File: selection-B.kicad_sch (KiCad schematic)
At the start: 11 parts, among them Q2 Q_NMOS_DGS, Q3 Q_NMOS_DGS, Q4 Q_NMOS_DGS, Q5 Q_NMOS_DGS, U11 SN74LS08N, U12 SN74LS08N, U13 CD74HCT32E, U9 SN74LS08N

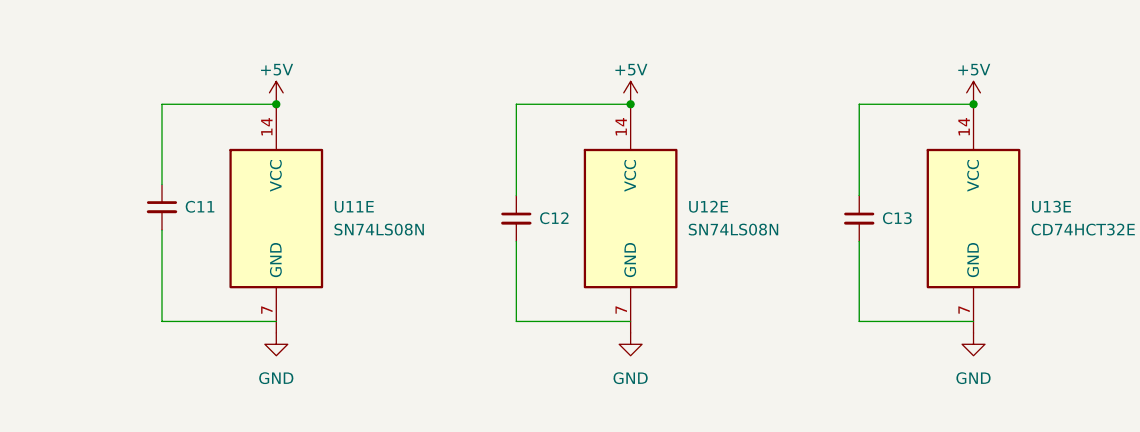
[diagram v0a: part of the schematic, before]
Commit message: fix: fixed link of capas
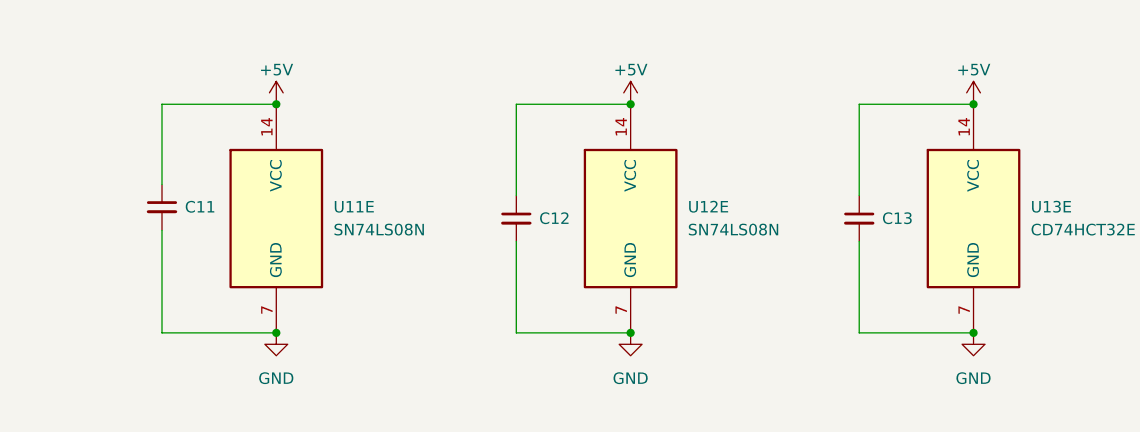
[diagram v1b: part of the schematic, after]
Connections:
- net GND: now also C11.2, C12.2, C13.2
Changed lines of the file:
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@@
+	)
+	(junction
+		(at 265.43 156.21)
+		(diameter 0)
+		(color 0 0 0 0)
+	)
+	(junction
+		(at 187.96 156.21)
+		(diameter 0)
+		(color 0 0 0 0)
 	)
 	(junction
@@
 		(color 0 0 0 0)
 	)
+	(junction
+		(at 227.33 156.21)
+		(diameter 0)
+		(color 0 0 0 0)
+	)
 	(wire
 		(pts
@@
 	(wire
 		(pts
-			(xy 187.96 154.94) (xy 175.26 154.94)
-		)
-		(stroke
-			(width 0)
-			(type default)
-		)
-	)
-	(wire
-		(pts
 			(xy 62.23 48.26) (xy 80.01 48.26)
 		)
@@
 	(wire
 		(pts
+			(xy 252.73 146.05) (xy 252.73 156.21)
+		)
+		(stroke
+			(width 0)
+			(type default)
+		)
+	)
+	(wire
+		(pts
 			(xy 101.6 93.98) (xy 105.41 93.98)
 		)
@@
 	(wire
 		(pts
-			(xy 175.26 154.94) (xy 175.26 144.78)
-		)
-		(stroke
-			(width 0)
-			(type default)
-		)
-	)
-	(wire
-		(pts
 			(xy 99.06 80.01) (xy 99.06 107.95)
 		)
@@
 	(wire
 		(pts
+			(xy 175.26 144.78) (xy 175.26 156.21)
+		)
+		(stroke
+			(width 0)
+			(type default)
+		)
+	)
+	(wire
+		(pts
 			(xy 101.6 38.1) (xy 105.41 38.1)
 		)
@@
 	(wire
 		(pts
-			(xy 252.73 154.94) (xy 252.73 146.05)
-		)
-		(stroke
-			(width 0)
-			(type default)
-		)
-	)
-	(wire
-		(pts
 			(xy 87.63 71.12) (xy 91.44 71.12)
 		)
@@
 	(wire
 		(pts
-			(xy 214.63 154.94) (xy 214.63 146.05)
-		)
-		(stroke
-			(width 0)
-			(type default)
-		)
-	)
-	(wire
-		(pts
 			(xy 124.46 49.53) (xy 120.65 49.53)
 		)
@@
 	(wire
 		(pts
+			(xy 214.63 146.05) (xy 214.63 156.21)
+		)
+		(stroke
+			(width 0)
+			(type default)
+		)
+	)
+	(wire
+		(pts
 			(xy 59.69 17.78) (xy 73.66 17.78)
 		)
@@
 	(wire
 		(pts
-			(xy 227.33 154.94) (xy 214.63 154.94)
-		)
-		(stroke
-			(width 0)
-			(type default)
-		)
-	)
-	(wire
-		(pts
 			(xy 99.06 52.07) (xy 105.41 52.07)
 		)
@@
 	(wire
 		(pts
-			(xy 265.43 154.94) (xy 252.73 154.94)
-		)
-		(stroke
-			(width 0)
-			(type default)
-		)
-	)
-	(wire
-		(pts
 			(xy 69.85 88.9) (xy 69.85 104.14)
 		)
@@
 	(wire
 		(pts
+			(xy 252.73 156.21) (xy 265.43 156.21)
+		)
+		(stroke
+			(width 0)
+			(type default)
+		)
+	)
+	(wire
+		(pts
 			(xy 139.7 69.85) (xy 143.51 69.85)
 		)
@@
 	(wire
 		(pts
+			(xy 214.63 156.21) (xy 227.33 156.21)
+		)
+		(stroke
+			(width 0)
+			(type default)
+		)
+	)
+	(wire
+		(pts
 			(xy 124.46 105.41) (xy 120.65 105.41)
 		)
 		(stroke
+			(width 0)
+			(type default)
+		)
+	)
+	(wire
+		(pts
+			(xy 175.26 156.21) (xy 187.96 156.21)
+		)
+		(stroke

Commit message: feat: updated references
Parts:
- C11, C12, C13: value C_Small -> CC0603KRX7R9BB104
- Q2, Q3, Q4, Q5: value Q_NMOS_DGS -> DMG2302U-7
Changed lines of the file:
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@@
 			)
 		)
-		(property "Value" "C_Small"
+		(property "Value" "CC0603KRX7R9BB104"
 			(at 217.17 144.7862 0)
 			(hide yes)
@@
 			)
 		)
-		(property "Value" "Q_NMOS_DGS"
+		(property "Value" "DMG2302U-7"
 			(at 82.55 41.402 0)
 			(show_name no)
@@
 			)
 		)
-		(property "Value" "Q_NMOS_DGS"
+		(property "Value" "DMG2302U-7"
 			(at 82.55 69.342 0)
 			(show_name no)
@@
 			)
 		)
-		(property "Value" "Q_NMOS_DGS"
+		(property "Value" "DMG2302U-7"
 			(at 82.55 97.282 0)
 			(show_name no)
@@
 			)
 		)
-		(property "Value" "C_Small"
+		(property "Value" "CC0603KRX7R9BB104"
 			(at 177.8 143.5162 0)
 			(hide yes)
@@
 			)
 		)
-		(property "Value" "Q_NMOS_DGS"
+		(property "Value" "DMG2302U-7"
 			(at 82.55 125.222 0)
 			(show_name no)
@@
 			)
 		)
-		(property "Value" "C_Small"
+		(property "Value" "CC0603KRX7R9BB104"
 			(at 255.27 144.7862 0)
 			(hide yes)

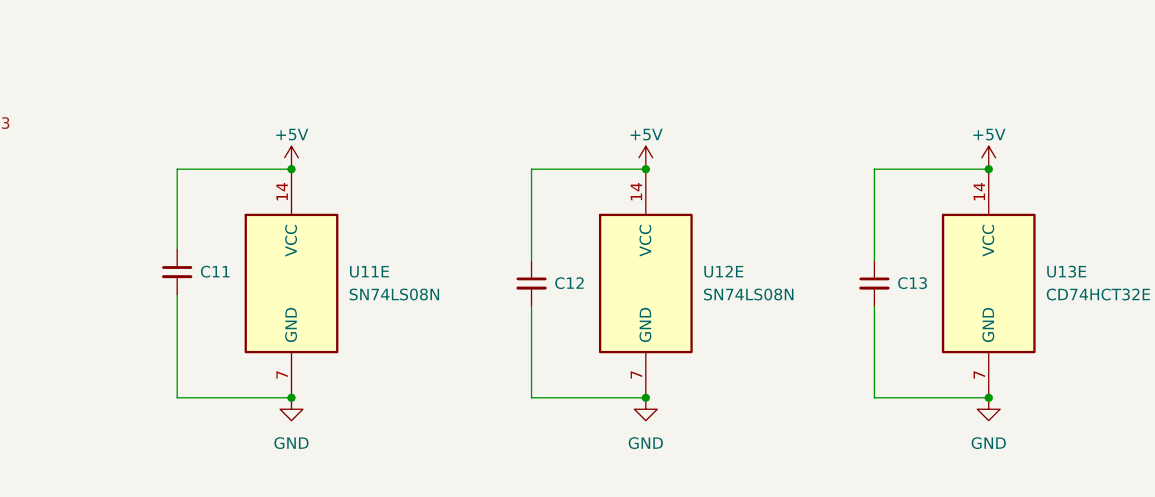
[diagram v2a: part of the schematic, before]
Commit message: Remove capacitors + change R and C footprints + finish PCB routing
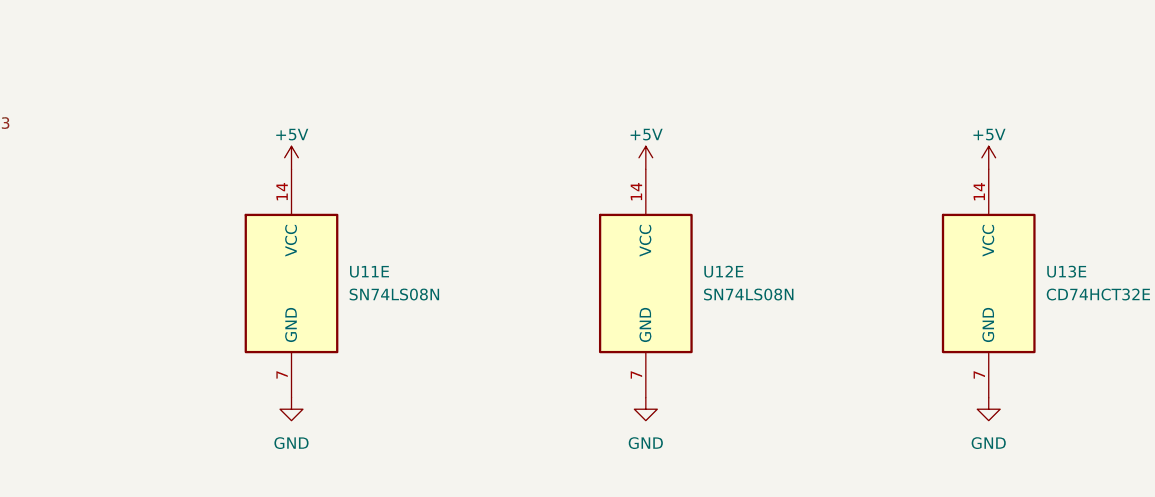
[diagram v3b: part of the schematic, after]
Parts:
- removed C11, C12, C13: CC0603KRX7R9BB104, Capacitor_SMD:C_0603_1608Metric_Pad1.08x0.95mm_HandSolder, symbol Device:C_Small

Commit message: fix: reput capas -- where is my gift?
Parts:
- added C11, C12, C13: C_Small, Capacitor_SMD:C_0603_1608Metric, symbol Device:C_Small
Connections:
- net +5V: now also C11.1, C12.1, C13.1
- net GND: now also C11.2, C12.2, C13.2

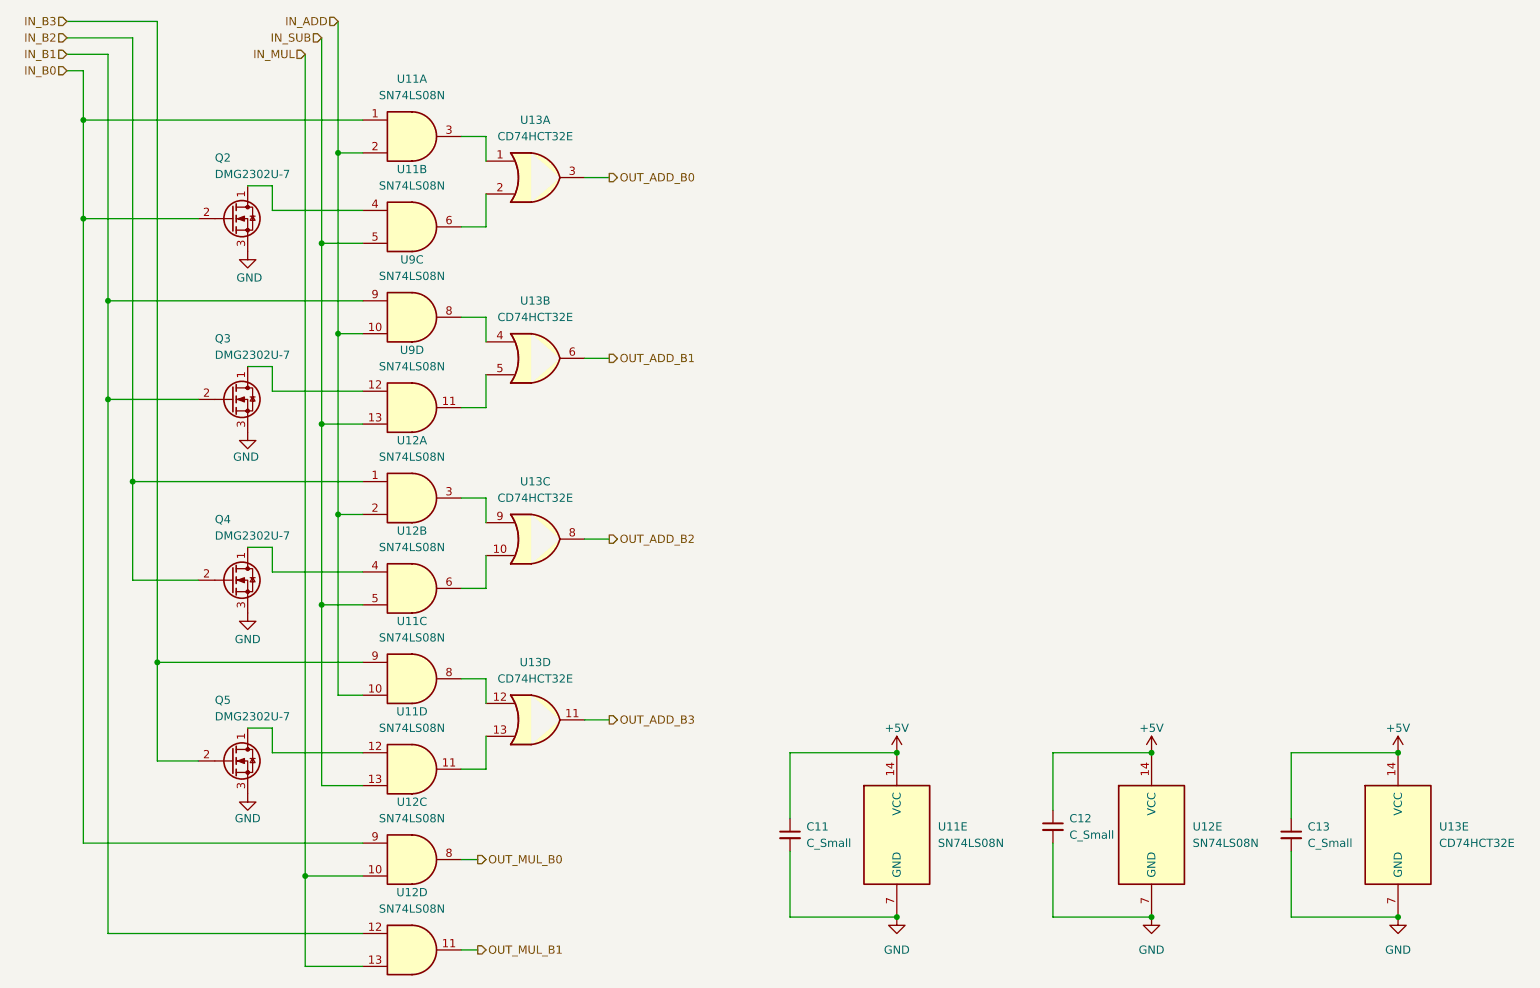
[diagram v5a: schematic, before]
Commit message: feat: missing pull up
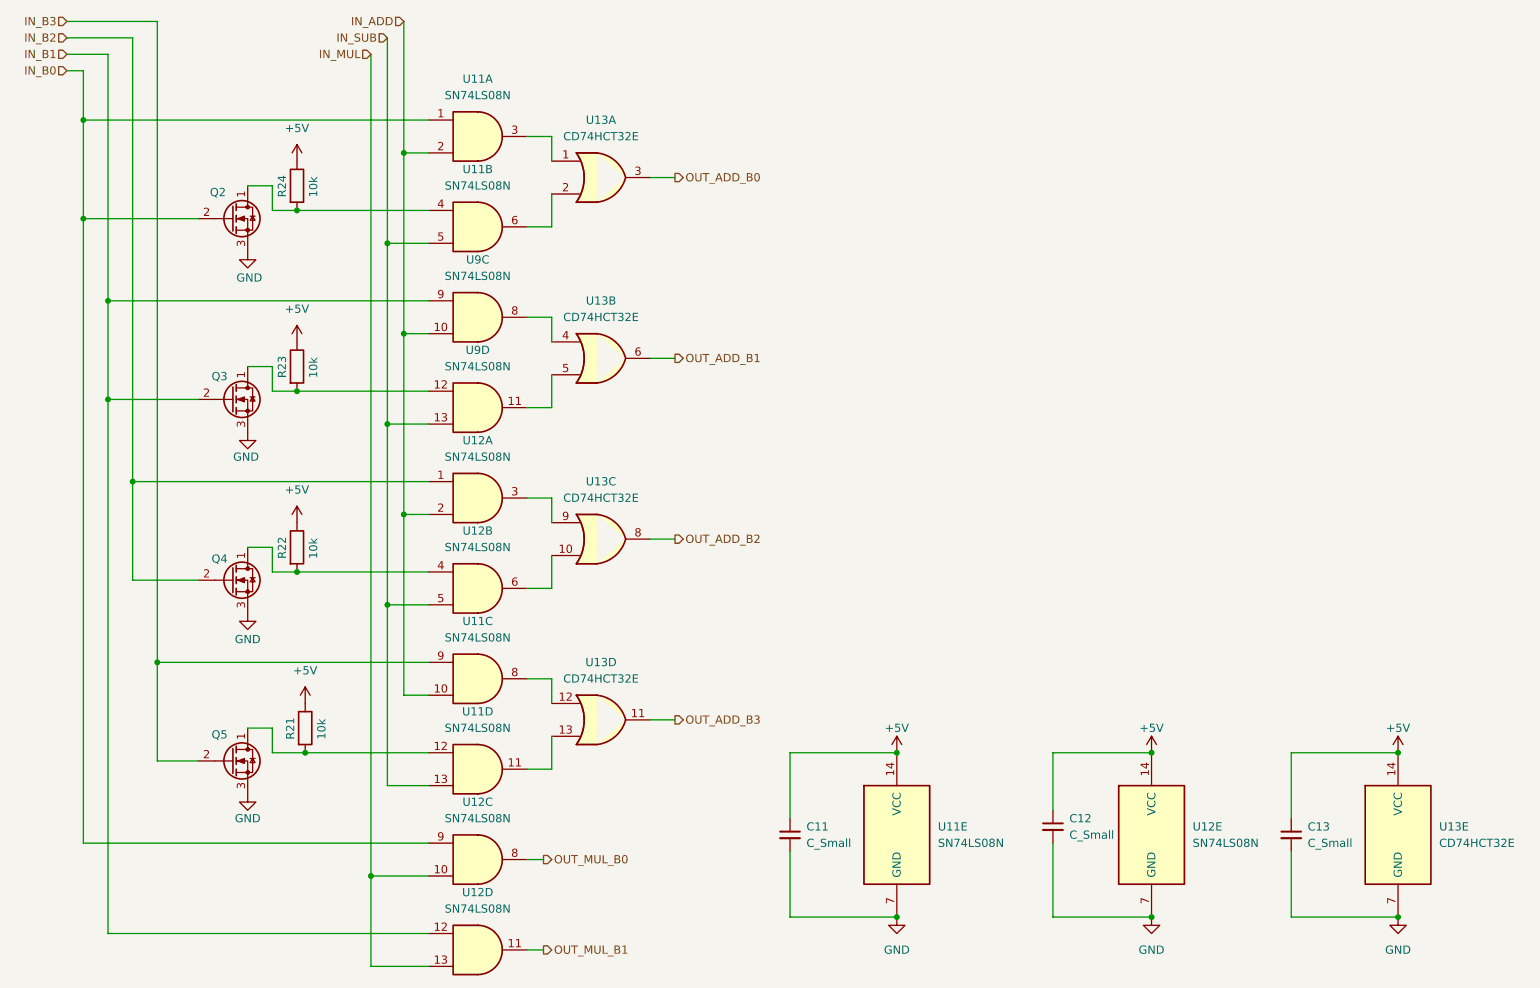
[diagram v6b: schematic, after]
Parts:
- added R21, R22, R23, R24: 10k, Resistor_SMD:R_0603_1608Metric_Pad0.98x0.95mm_HandSolder, symbol Device:R
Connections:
- net +5V: now also R21.1, R22.1, R23.1, R24.1
- net at Q4.1 (D), U12.4: now also R22.2
- net at Q5.1 (D), U11.12: now also R21.2
- net at Q2.1 (D), U11.4: now also R24.2
- net at Q3.1 (D), U9.12: now also R23.2
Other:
- moved on the sheet: U11A, U11B, U11C, U11D, U12A, U12B, U12C, U12D, U13A, U13B, U13C, U13D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

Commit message: feat: multiplier schema
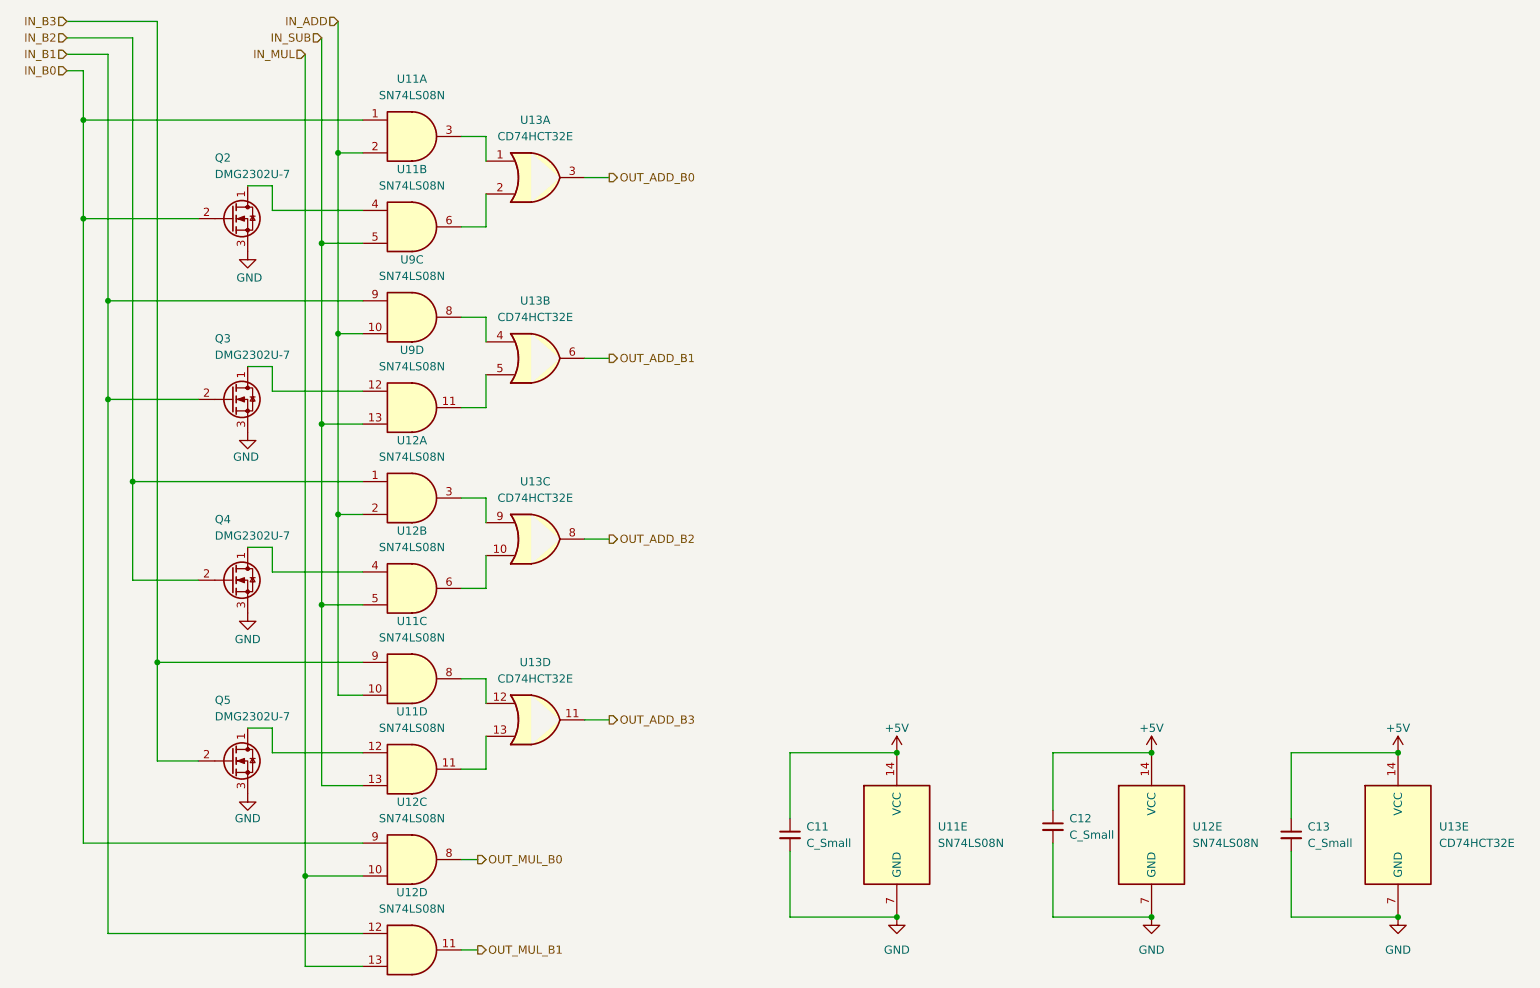
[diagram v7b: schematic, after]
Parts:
- removed R21, R22, R23, R24: 10k, Resistor_SMD:R_0603_1608Metric_Pad0.98x0.95mm_HandSolder, symbol Device:R
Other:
- moved on the sheet: U11A, U11B, U11C, U11D, U12A, U12B, U12C, U12D, U13A, U13B, U13C, U13D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
